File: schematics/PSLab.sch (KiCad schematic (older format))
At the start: 193 parts, among them J1 DoublePins, J11 Li-Ion Battery, J2 Power Pins, J3 Wave Generator, J4 I2C, J5 I2C, J6 ESP01, J7 UART, J8 Battery Switch, J9 SPI, P1 SDCard, P2 USB_C - Generic, Q1 MMBT3906, Q2 MMBT3904, Q3 MMBT3906, SW1 SW_MEC_5E, SW2 SW_MEC_5E, SW3 SW_MEC_5E, U1 FP6291, U10 TL082, U11 TL082, U12 74HC4051, U13 MAX5400, U14 MAX5400, U15 CP2102N-xxx-xQFN20x, U16 SP0503BAHT, U17 IP5189T, U18 TL082, U19 MCP4822, U2 74HC126, U20 MCP4822, U3 PIC24EP256GP204, U4 DS1307Z+, U5 TP7660H, U6 HT7333-A, U7 LM324, U8 TL082, U9 TL082, X2 32.768 kHz, Y1 12 MHz

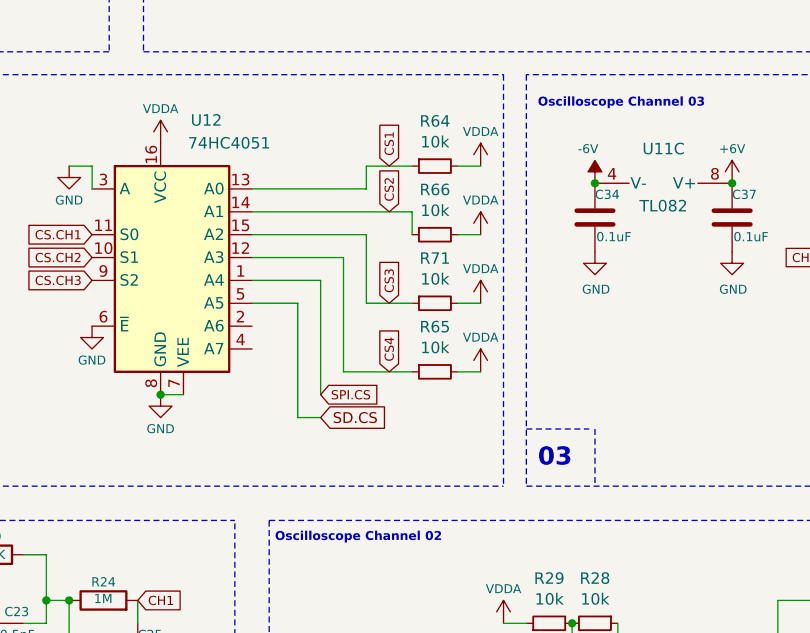
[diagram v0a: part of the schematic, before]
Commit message: chore: add pull-up resistors to SPI_CS SD_CS pins
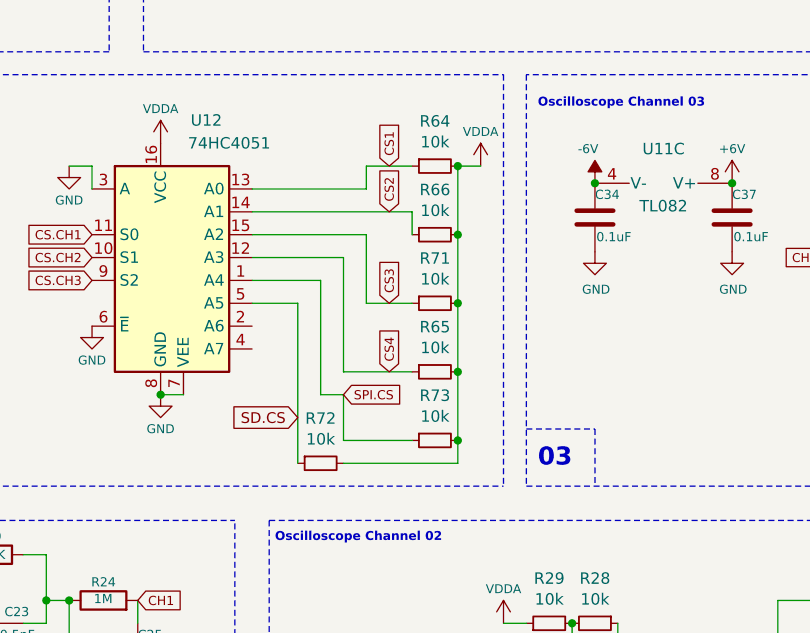
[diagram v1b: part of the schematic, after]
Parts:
- added R72, R73: 10k, Resistor_SMD:R_0603_1608Metric, symbol Device:R_Small
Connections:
- wire segments 468 -> 473
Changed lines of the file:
@@
 Text GLabel 10500 4600 0    40   Input ~ 0
 CS.CH3
-Text GLabel 19200 5400 2    40   Input ~ 0
+Text GLabel 19300 5400 2    40   Input ~ 0
 SPI.CS
 Text GLabel 10550 3400 0    40   Input ~ 0
@@
 03
 Wire Notes Line style solid rgb(255, 0, 0)
-	20100 5550 20375 5550
+	20100 5550 20400 5550
 Wire Notes Line style solid rgb(255, 0, 0)
 	20400 5550 20400 5800
@@
 $EndComp
 $Comp
-L power:VDDA #PWR091
-U 1 1 61D5A696
-P 19900 4700
-F 0 "#PWR091" H 19900 4550 50  0001 C CNN
-F 1 "VDDA" H 19900 4850 39  0000 C CNN
-F 2 "" H 19900 4700 50  0001 C CNN
-F 3 "" H 19900 4700 50  0001 C CNN
-	1    19900 4700
-	-1   0    0    -1
-$EndComp
-Wire Wire Line
-	19900 4700 19800 4700
-$Comp
 L Device:R_Small R65
 U 1 1 61E93C79
@@
 	0    -1   1    0
 $EndComp
-$Comp
-L power:VDDA #PWR0155
-U 1 1 62020B48
-P 19900 5000
-F 0 "#PWR0155" H 19900 4850 50  0001 C CNN
-F 1 "VDDA" H 19900 5150 39  0000 C CNN
-F 2 "" H 19900 5000 50  0001 C CNN
-F 3 "" H 19900 5000 50  0001 C CNN
-	1    19900 5000
-	-1   0    0    -1
-$EndComp
-Wire Wire Line
-	19900 5000 19800 5000
-$Comp
-L power:VDDA #PWR054
-U 1 1 620E21AE
-P 19900 5300
-F 0 "#PWR054" H 19900 5150 50  0001 C CNN
-F 1 "VDDA" H 19900 5450 39  0000 C CNN
-F 2 "" H 19900 5300 50  0001 C CNN
-F 3 "" H 19900 5300 50  0001 C CNN
-	1    19900 5300
-	-1   0    0    -1
-$EndComp
-Wire Wire Line
-	19900 5300 19800 5300
 Text GLabel 21400 1100 0    40   Input ~ 0
 SCK
@@
 Wire Wire Line
 	18900 4900 19200 4900
-Text GLabel 19200 5500 2    47   Input ~ 0
+Text GLabel 19100 5500 0    47   Input ~ 0
 SD.CS
 Wire Wire Line
 	18900 5000 19100 5000
 Wire Wire Line
-	19100 5000 19100 5500
-Wire Wire Line
-	19100 5500 19200 5500
-Wire Wire Line
 	18600 2000 18800 2000
 Wire Wire Line
 	20800 2800 21000 2800
+$Comp
+L Device:R_Small R73
+U 1 1 61DC97A5
+P 19700 5600
+F 0 "R73" V 19504 5600 50  0000 C CNN
+F 1 "10k" V 19595 5600 50  0000 C CNN
+F 2 "Resistor_SMD:R_0603_1608Metric" H 19700 5600 50  0001 C CNN
+F 3 "~" H 19700 5600 50  0001 C CNN
+	1    19700 5600
+	0    -1   1    0
+$EndComp
+$Comp
+L Device:R_Small R72
+U 1 1 61DCA3AE
+P 19200 5700
+F 0 "R72" V 19004 5700 50  0000 C CNN
+F 1 "10k" V 19095 5700 50  0000 C CNN
+F 2 "Resistor_SMD:R_0603_1608Metric" H 19200 5700 50  0001 C CNN
+F 3 "~" H 19200 5700 50  0001 C CNN
+	1    19200 5700
+	0    -1   1    0
+$EndComp
+Wire Wire Line
+	19800 4400 19800 4700
+Connection ~ 19800 4400
+Connection ~ 19800 4700
+Wire Wire Line
+	19800 4700 19800 5000
+Connection ~ 19800 5000
+Wire Wire Line
+	19800 5000 19800 5300
+Connection ~ 19800 5300
+Wire Wire Line
+	19800 5300 19800 5600
+Wire Wire Line
+	19200 5400 19300 5400
+Wire Wire Line
+	19300 5400 19300 5600
+Wire Wire Line
+	19300 5600 19600 5600
+Wire Wire Line
+	19100 5000 19100 5700
+Wire Wire Line
+	19300 5700 19800 5700
+Wire Wire Line
+	19800 5700 19800 5600
+Connection ~ 19800 5600
 $EndSCHEMATC

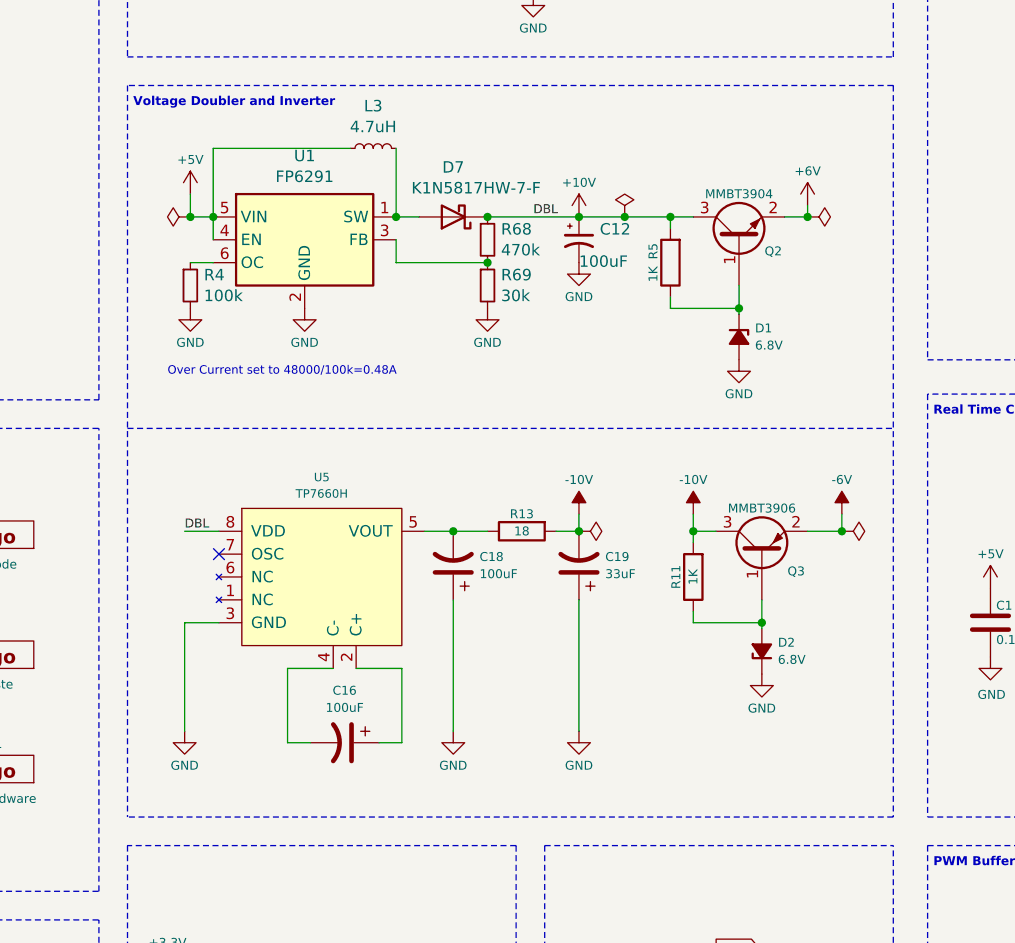
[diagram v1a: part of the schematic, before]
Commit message: Remove all 100uF capcitors
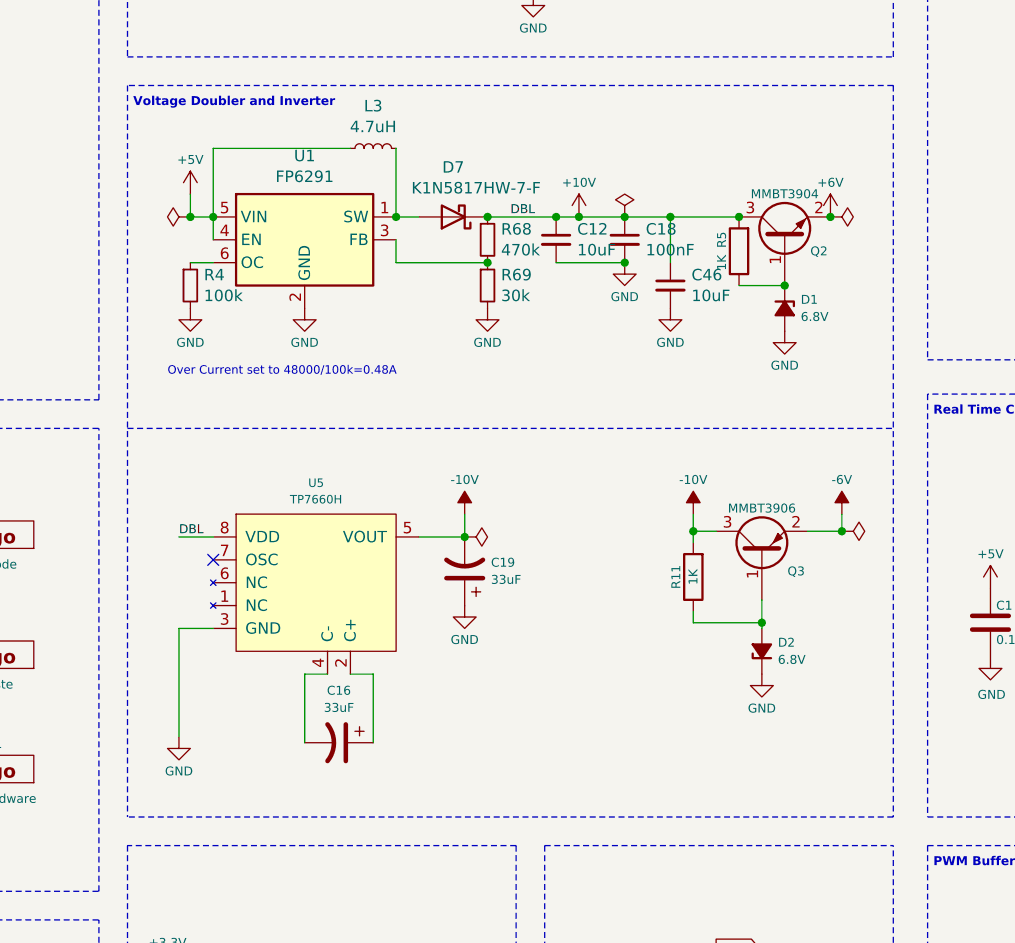
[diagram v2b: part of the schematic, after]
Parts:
- removed C12: 100uF, Capacitor_Tantalum_SMD:CP_EIA-3528-21_Kemet-B, symbol Device:CP1_Small
- removed C18: 100uF, Capacitor_Tantalum_SMD:CP_EIA-6032-28_Kemet-C, symbol Device:CP1
- removed R13: 18, Resistor_SMD:R_0603_1608Metric, symbol Device:R
- added C12, C46: 10uF, Capacitor_SMD:C_0603_1608Metric, symbol Device:C_Small
- added C18: 100nF, Capacitor_SMD:C_0603_1608Metric, symbol Device:C_Small
- C16: value 100uF -> 33uF; footprint Capacitor_Tantalum_SMD:CP_EIA-6032-28_Kemet-C -> Capacitor_Tantalum_SMD:CP_EIA-3528-21_Kemet-B
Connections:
- wire segments 473 -> 464
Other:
- moved on the sheet: C16, C19, D1, Q2, R5, U5

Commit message: Temp9
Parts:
- removed J11: Li-Ion Battery, Connector_PinHeader_2.54mm:PinHeader_1x02_P2.54mm_Vertical, symbol Connector_Generic:Conn_01x02
- removed J8: Battery Switch, Connector_PinHeader_2.54mm:PinHeader_1x02_P2.54mm_Vertical, symbol Connector_Generic:Conn_01x02
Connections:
- wire segments 464 -> 454
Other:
- moved on the sheet: BT1, BT3, U4, X2

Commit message: refactor: replace IP5189T to IP5219T
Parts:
- removed R61: 200k, Resistor_SMD:R_0603_1608Metric, symbol Device:R_Small
- removed U17: IP5189T, Package_DFN_QFN:QFN-24-1EP_4x4mm_P0.5mm_EP2.6x2.6mm, symbol PSLab:IP5189T
- added D6: GREEN, LED_SMD:LED_0805_2012Metric, symbol Device:LED_ALT
- added R13: 5.1k, Resistor_SMD:R_0603_1608Metric, symbol Device:R_Small
- added U21: IP5219, Package_DFN_QFN:QFN-24-1EP_4x4mm_P0.5mm_EP2.6x2.6mm, symbol PSLab:IP5219
- R63: value 51k -> 0
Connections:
- wire segments 454 -> 449
- no-connect marks 30 -> 29
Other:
- note removed: "I_chg=1.2V / R_chg*100000=0.6A"
- moved on the sheet: R63
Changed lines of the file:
@@
 Data
 89 50 4E 47 0D 0A 1A 0A 00 00 00 0D 49 48 44 52 00 00 02 08 00 00 00 CC 08 03 00 00 00 21 C4 AB
-DA 00 00 00 03 73 42 49 54 08 08 08 DB E1 4F E0 00 00 03 00 50 4C 54 45 01 00 00 FF FF E2 79 5D
+DA 00 00 00 03 73 42 49 54 08 08 08 DB E1 4F E0 00 00 03 00 50 4C 54 45 02 00 00 FF FF E2 79 5D
 9D 28 5D A5 28 7D CE E2 FF FF 81 5D B6 A5 EA FF C6 99 A5 28 99 E2 FF EA D6 59 5D C2 C6 FF FF 59
 B6 F2 FF FF F2 A5 7D A5 28 5D C6 E2 B6 B6 81 CE FF FF CE C6 81 7D D6 55 5D A1 59 7D BE F6 F6 F6
@@
 F6 99 D2 CE 40 9D D6 EA EE F6 40 5D A5 28 5D BA 7D D2 DE 55 AE DE 28 75 C2 CA DA EA 99 AA B6 65
 C2 DE 85 A5 CA 4C 4C 4C A1 A1 A1 3C 3C 3C 61 65 69 A5 B2 BE 85 A1 CE 91 99 A1 EE F2 F2 7D 81 81
-B6 BE C6 91 91 91 7D 7D 81 50 79 B6 C2 C2 C2 99 B2 7D 5D B6 DE FA FA FA 76 CF DF 8C 00 00 00 01
+B6 BE C6 91 91 91 7D 7D 81 50 79 B6 C2 C2 C2 99 B2 7D 5D B6 DE FA FA FA 4A AB 90 C2 00 00 00 01
 74 52 4E 53 00 40 E6 D8 66 00 00 15 08 49 44 41 54 78 9C ED 9D 7B 80 15 D5 79 C0 67 99 A5 31 A6
 26 05 83 EC 2E FB 76 60 9B 44 F6 01 BB CA 43 77 F7 C6 18 1F 10 31 36 1B 5D 4C 82 69 D6 24 D6 A0
@@
 $EndComp
 $Comp
-L Device:R_Small R61
-U 1 1 61CE626C
-P 1200 4800
-F 0 "R61" H 1259 4846 50  0000 L CNN
-F 1 "200k" H 1259 4755 50  0000 L CNN
-F 2 "Resistor_SMD:R_0603_1608Metric" H 1200 4800 50  0001 C CNN
-F 3 "~" H 1200 4800 50  0001 C CNN
-	1    1200 4800
-	1    0    0    -1
-$EndComp
-$Comp
 L power:GND #PWR0105
 U 1 1 61D97D5A
@@
 L power:GND #PWR0150
 U 1 1 61D98315
-P 1200 5100
-F 0 "#PWR0150" H 1200 4850 50  0001 C CNN
-F 1 "GND" H 1205 4927 50  0000 C CNN
-F 2 "" H 1200 5100 50  0001 C CNN
-F 3 "" H 1200 5100 50  0001 C CNN
-	1    1200 5100
+P 1300 5200
+F 0 "#PWR0150" H 1300 4950 50  0001 C CNN
+F 1 "GND" H 1305 5027 50  0000 C CNN
+F 2 "" H 1300 5200 50  0001 C CNN
+F 3 "" H 1300 5200 50  0001 C CNN
+	1    1300 5200
 	1    0    0    -1
 $EndComp
@@
 Wire Wire Line
 	2100 4200 2100 4100
-NoConn ~ 3100 5200
+NoConn ~ 3100 5300
 Wire Wire Line
 	3100 4100 3200 4100
@@
 Text Label 1900 4100 0    39   ~ 0
 VINPUT
-Connection ~ 2100 4100
-Connection ~ 3100 4400
-Wire Wire Line
-	3100 4400 3100 4300
-Wire Wire Line
-	3100 4500 3100 4400
-Connection ~ 2100 5500
-Connection ~ 2100 5400
-Wire Wire Line
-	2100 5400 2100 5500
-Wire Wire Line
-	2100 5300 2100 5400
-$Comp
-L PSLab:IP5189T U17
-U 1 1 61BDEDE0
-P 2400 4000
-F 0 "U17" H 2600 4136 37  0000 C CNN
-F 1 "IP5189T" H 2600 4064 37  0000 C CNN
-F 2 "Package_DFN_QFN:QFN-24-1EP_4x4mm_P0.5mm_EP2.6x2.6mm" H 2700 2300 37  0001 C CNN
-F 3 "http://www.injoinic.com/wwwroot/uploads/files/20200220/3642884e4c0184d6c0173a5193cd56ce.pdf" H 4300 2600 37  0001 C CNN
-	1    2400 4000
-	1    0    0    -1
-$EndComp
 Connection ~ 3800 4300
 Wire Wire Line
@@
 Wire Wire Line
 	3100 4300 3200 4300
-Connection ~ 3100 4300
 Wire Wire Line
 	3100 4600 3300 4600
@@
 Wire Wire Line
 	1900 4100 2100 4100
-NoConn ~ 3100 5300
 NoConn ~ 3100 5400
 NoConn ~ 3100 5500
 NoConn ~ 3100 4800
 NoConn ~ 3100 4900
-Text Notes 800  4700 0    37   ~ 0
-I_chg=1.2V / R_chg*100000=0.6A
 Wire Wire Line
 	5600 5800 5700 5800
@@
 $EndComp
 Connection ~ 1500 5300
-Wire Wire Line
-	1200 4700 2000 4700
-Wire Wire Line
-	2000 4700 2000 4800
-Wire Wire Line
-	2000 4800 2100 4800
-Wire Wire Line
-	2100 5000 2000 5000
-Wire Wire Line
-	2000 5000 2000 4900
 $Comp
 L Device:R_Small R63
 U 1 1 62134A7C
-P 1300 5000
-F 0 "R63" H 1359 5046 50  0000 L CNN
-F 1 "51k" H 1359 4955 50  0000 L CNN
-F 2 "Resistor_SMD:R_0603_1608Metric" H 1300 5000 50  0001 C CNN
-F 3 "~" H 1300 5000 50  0001 C CNN
-	1    1300 5000
+P 1300 5100
+F 0 "R63" H 1359 5146 50  0000 L CNN
+F 1 "0" H 1359 5055 50  0000 L CNN
+F 2 "Resistor_SMD:R_0603_1608Metric" H 1300 5100 50  0001 C CNN
+F 3 "~" H 1300 5100 50  0001 C CNN
+	1    1300 5100
 	1    0    0    -1
 $EndComp
-Wire Wire Line
-	1200 4900 1200 5100
-Wire Wire Line
-	1200 5100 1300 5100
-Connection ~ 1200 5100
 $Comp
 L Device:R R16
@@
 	3900 4300 4300 4300
 $Comp
-L power:GND #PWR?
+L power:GND #PWR054
 U 1 1 62AD1385
 P 4300 4600
-F 0 "#PWR?" H 4300 4350 50  0001 C CNN
+F 0 "#PWR054" H 4300 4350 50  0001 C CNN
 F 1 "GND" H 4305 4427 50  0000 C CNN
 F 2 "" H 4300 4600 50  0001 C CNN
@@
 	1    0    0    -1
 $EndComp
+$Comp
+L PSLab:IP5219 U21
+U 1 1 61CBED2B
+P 2400 4000
+F 0 "U21" H 2600 4136 37  0000 C CNN
+F 1 "IP5219" H 2600 4064 37  0000 C CNN
+F 2 "Package_DFN_QFN:QFN-24-1EP_4x4mm_P0.5mm_EP2.6x2.6mm" H 2700 2400 37  0001 C CNN
+F 3 "http://www.injoinic.com/wwwroot/uploads/files/20200220/3642884e4c0184d6c0173a5193cd56ce.pdf" H 4300 2600 37  0001 C CNN
+	1    2400 4000
+	1    0    0    -1
+$EndComp
+$Comp
+L Device:LED_ALT D6
+U 1 1 61CF3FE2
+P 3650 5200
+F 0 "D6" H 3775 5150 39  0000 C CNN
+F 1 "GREEN" H 3475 5250 39  0000 C CNN
+F 2 "LED_SMD:LED_0805_2012Metric" H 3650 5200 50  0001 C CNN
+F 3 "https://eu.mouser.com/datasheet/2/678/av02-0977en-1827813.pdf" H 3650 5200 50  0001 C CNN
+F 4 "Green 0805" H 3650 5200 50  0001 C CNN "Description"
+F 5 "HSMQ-C170-T0000" H 3650 5200 50  0001 C CNN "Mfr No."
+F 6 "HSMQ-C170-T0000" H 3650 5200 50  0001 C CNN "PartNumber"
+F 7 "0.94" H 3650 5200 50  0001 C CNN "Price"
+	1    3650 5200
+	-1   0    0    1
+$EndComp
+Wire Wire Line
+	3100 5200 3300 5200
+$Comp
+L power:GND #PWR053
+U 1 1 61D3A097
+P 4000 5200
+F 0 "#PWR053" H 4000 4950 50  0001 C CNN
+F 1 "GND" H 4005 5027 50  0000 C CNN
+F 2 "" H 4000 5200 50  0001 C CNN
+F 3 "" H 4000 5200 50  0001 C CNN
+	1    4000 5200
+	1    0    0    -1
+$EndComp
+$Comp
+L Device:R_Small R13
+U 1 1 61D3A38D
+P 3400 5200
+F 0 "R13" H 3459 5246 50  0000 L CNN
+F 1 "5.1k" H 3459 5155 50  0000 L CNN
+F 2 "Resistor_SMD:R_0603_1608Metric" H 3400 5200 50  0001 C CNN
+F 3 "~" H 3400 5200 50  0001 C CNN
+	1    3400 5200
+	0    1    1    0
+$EndComp
+Wire Wire Line
+	1300 5000 2100 5000
+Wire Wire Line
+	2100 5300 2100 5400
+Wire Wire Line
+	3100 4400 3100 4500
+Connection ~ 2100 4100
+Wire Wire Line
+	3100 4300 3100 4400
+Connection ~ 3100 4300
+Connection ~ 3100 4400
+Wire Wire Line
+	2100 5400 2100 5500
+Connection ~ 2100 5400
+Connection ~ 2100 5500
 Wire Wire Line
-	1300 4900 2000 4900
+	3800 5200 4000 5200
 $EndSCHEMATC

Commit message: chore: modify 0.1uF to 100nF
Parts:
- C1, C13, C17, C2, C22, C24, C25, C26, C27, C28, C3, C31, C32, C34, C35, C37, C38, C39, C4, C41, C43, C5, C9: value 0.1uF -> 100nF
- R12, R15, R2, R26, R3, R41, R43, R44, R48, R52, R53, R59, R60: value 5K1 -> 5.1k

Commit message: chore: modify tf card slot
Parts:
- removed P1: SDCard, PSLab:microSD_HC_Hirose_DM3AT-SF-PEJM5, symbol PSLab:SDCard
- removed Y1: 12 MHz, Crystal:Crystal_SMD_3225-4Pin_3.2x2.5mm, symbol Device:Crystal_GND24_Small
- added C47: 33uF, Capacitor_Tantalum_SMD:CP_EIA-3528-21_Kemet-B, symbol Device:CP1_Small
- added J8: Micro_SD_Card_Det_9_pin, PSLab:TF-015, symbol PSLab:Micro_SD_Card_Det_9_pin
- added Y1: 12MHz, Crystal:Crystal_SMD_5032-2Pin_5.0x3.2mm, symbol Device:Crystal
- L1: value 10uH -> 4.7uH
- L2, L3: value 4.7uH -> 3.3uH
- R1, R10, R14, R16, R17, R18, R19, R21, R25, R31, R32, R33, R35, R37, R38, R39, R42, R58, R67: value 10K -> 10k
- TP1, TP2, TP3, TP5, TP6: footprint PSLab:Voltage_Test_Point -> PSLab:Test_Point_0.8mm
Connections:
- net labels removed: DBL
- wire segments 449 -> 445
- no-connect marks 29 -> 28
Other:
- moved on the sheet: C46, D1, MH1, MH2, MH3, MH4, Q2, R5

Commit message: refactor: replace IP5219 to IP51289T
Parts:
- removed U21: IP5219, Package_DFN_QFN:QFN-24-1EP_4x4mm_P0.5mm_EP2.6x2.6mm, symbol PSLab:IP5219
- added R61: 51k, Resistor_SMD:R_0603_1608Metric, symbol Device:R_Small
- added R74: 1k, Resistor_SMD:R_0603_1608Metric, symbol Device:R_Small
- added U21: IP5189T, Package_DFN_QFN:QFN-24-1EP_4x4mm_P0.5mm_EP2.6x2.6mm, symbol PSLab:IP5189T
- R63: value 0 -> 200k
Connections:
- net labels added: LD3
- wire segments 445 -> 456
- no-connect marks 28 -> 26
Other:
- note added: "I_chg=1.2V / R_chg*100000=0.6A"
- moved on the sheet: BT3, C11, C14, C45, D6, L2, R13, R62, R63, SW3

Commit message: 20220302, send to manufacturer
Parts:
- removed C46: 10uF, Capacitor_SMD:C_0603_1608Metric, symbol Device:C_Small
- removed R22, R29: 10k, Resistor_SMD:R_0603_1608Metric, symbol Device:R_Small
- added C48: 22uF, Capacitor_SMD:C_0603_1608Metric, symbol Device:C_Small
- added R22: 12k, Resistor_SMD:R_0603_1608Metric, symbol Device:R
- added R29: 10k, Resistor_SMD:R_0603_1608Metric, symbol Device:R
- C23, C29: value 0.5pF -> 1pF
- L1: value 4.7uH -> 3.3uH
- L2: value 3.3uH -> 4.7uH
- R20, R30: value 200K -> 100k
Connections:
- net +3V3: now also R64.2, R65.2, R66.2, R71.2, R72.2, R73.2, U12.16 (VCC)
- net +6V: now also U18.8 (V+)
- net -6V: now also U18.4 (V-)
- net DAC.1: now also U20.8 (VA); no longer U20.6 (VB)
- net DAC.2: now also U20.6 (VB); no longer U20.8 (VA)
- net DAC.4: now also U19.6 (VB); no longer U19.8 (VA)
- net GND: now also C48.2, R29.2; no longer U18.4 (V-), U8.3 (+), U9.5 (+)
- net PVS3: now also U19.8 (VA); no longer U19.6 (VB)
- net VDDA: now also C48.1, R22.2; no longer R64.2, R65.2, R66.2, R71.2, R72.2, R73.2, U12.16 (VCC), U18.8 (V+)
- net at SW3.3 (K): now also SW3.4 (A), U21.8 (KEY)
- net at U13.7 (W): now also U8.2 (-); no longer U8.6 (-)
- net at R23.1, U13.8 (H): now also U8.1; no longer U8.7
- net at C23.1, R20.2: now also U13.1 (L), U8.7; no longer U8.1, U8.5 (+)
- net OSC_REF2: now reaches U18.1, U18.2 (-)
- net OSC_REF2: now also U8.5 (+), U9.5 (+)
- net at C29.1, R30.1, U9.7: now also U14.1 (L); no longer U9.3 (+)
- net at C23.2, R20.1, R24.1: now also U8.6 (-); no longer U8.2 (-)
- removed net OSC_REF: U13.1 (L), U14.1 (L), U18.3 (+), U18.6 (-), U18.7
- new net: R22.1, R29.1, U18.3 (+)
- new net OSC_REF1: U18.6 (-), U18.7, U8.3 (+), U9.3 (+)
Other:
- note added: "1.50V"
- note added: "1.65V"
- moved on the sheet: C12, C18, C22, C26, C28, C31, C39, C41, C47, D7, L3, R16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
